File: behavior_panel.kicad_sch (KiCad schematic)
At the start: 32 parts, among them J1 Conn_01x16, Q1 Q_NPN_BEC, Q3 N-channel MOSFET, U1 LM2902, U2 LM317_3PinPackage, U3 SFH617A-1X007T

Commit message: Add documentation to schematic
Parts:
- removed Q1: Q_NPN_BEC, Package_TO_SOT_SMD:SOT-23, symbol Device:Q_NPN_BEC
- removed R19: 10k, Resistor_SMD:R_0402_1005Metric, symbol Device:R
- removed U3: SFH617A-1X007T, Package_DIP:SMDIP-4_W9.53mm_Clearance8mm, symbol Isolator:SFH617A-1X007T
- added C7: 0.1uF, Capacitor_SMD:C_0805_2012Metric, symbol Device:C
- added C8: 1uF, Capacitor_SMD:C_0603_1608Metric, symbol Device:C
- added D1: LED, symbol Device:LED
- added Q2: N-channel MOSFET, Package_TO_SOT_SMD:TO-252-2, symbol Transistor_FET:BUZ11
- added Q4: N MOSFET, Package_TO_SOT_SMD:TO-252-2, symbol Transistor_FET:BUZ11
- added Q5: Q_NPN_BCE, symbol Device:Q_NPN_BCE
- added R11, R13: 10k, Resistor_SMD:R_0402_1005Metric, symbol Device:R
- added R12, R14: 50, Resistor_SMD:R_0402_1005Metric, symbol Device:R
- added R15: 1k, symbol Device:R
- added R16: 100, symbol Device:R
- added SW1: SW_SPST, symbol Switch:SW_SPST
- added U3: LM317_3PinPackage, Package_TO_SOT_SMD:SOT-223, symbol Regulator_Linear:LM317_3PinPackage
- R10: value 220 -> 860
- R9: value 10k -> 100; footprint Resistor_SMD:R_0402_1005Metric -> Resistor_SMD:R_0805_2012Metric; MPN MF-RES-0402-10k -> MF-RES-0805-100
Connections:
- net +28V: now also C7.1, U3.3 (VI); no longer R9.2
- net 5V: now also R16.1
- net GND: now also R10.2, C7.2, C8.2, Q2.3 (S), Q4.3 (S), Q5.3 (E), R11.2, R13.2, SW1.1 (A)
- net PD_CTL: no longer R10.1
- net PD_OUT: no longer R9.1
- new net: Q5.1 (B), R15.2
- new net: R10.1, R9.2, U3.1 (ADJ)
- new net: D1.1 (K), Q5.2 (C)
- new net: D1.2 (A), R16.2
- new net 12V: C8.1, R12.1, R14.1, R9.1, U3.2 (VO)
- new net S1_CTL: Q2.1 (G), R11.1
- new net S1_IN: Q2.2 (D)
- new net S1_OUT: R12.2
- new net S2_CTL: Q4.1 (G), R13.1
- new net S2_IN: Q4.2 (D), R15.1, SW1.2 (B)
- new net S2_OUT: R14.2
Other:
- note added: "E1+ and E2+ go to the positive (anode) of the IR emitter. Cathode goes to ground. S1+ and S2+ go to either leg of the IR sensor. Other leg goes to ground. The RC circuit (R7 and C1) feeding to the positive leg of the op-amp form a lowpass circuit (1/2piRC) with a current cutoff of 160 Hz. The feedback capacitor (C3) stabilizes the response of the op-amp. O1 and O2 would feed into a BNC output tha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"
- note added: "Ground (negative) side of light should be connected to LT_IN. This circuit is designed for a 3W DC 12-24V LED lamp (e.g., SKU: P-AL-3W-E27-CW-1224 from 12vmonster.com). Positive end of light should be connected to 12-24V output. Feed LT_IN and 12V into a BNC connector so we can plug the light directly into the box."
- note added: "In general, I favor putting in PBC traces to a 2.54mm pin header that way we don't have to deal with identifying connectors that can be soldered onto a PCB. Instead, we put the connectors on the box itself, solder wires that terminate in a 2.54mm pin shroud, mount the PCB in the box, and then hook up the connectors to the PCB by plugging into the pin header."
- note added: "This is meant to be the control circuit for one of the solenoids. The solenoids need 12V for power (not sure what current draw is). S2_CTL can be connected to the NI digital output so that we can control via software. S2_OUT goes to the positive input to the solenoid. S2_IN comes from the negative input of the solenoid. When S2_CTL is high, this should allow current to flow through the MOSFET (an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"
- note added: "Voltage regulator circuit. It might be worth keeping both the 5 and 12V rails that way we can power the circuit from any DC power supply that is at least 14V (min dropout is ~1.2V)."
- note removed: "* R7+C1 form a lowpass circuit with fc = 1/(2piRC). Selected values give us a cutoff of 160 Hz. * C3 helps stabilize the response of the op-amp. * C5 and C17 are power supply bypass. Resistors * R1 selected to provide a current of less than 50mA to IR LED."
- moved on the sheet: C11, C12, H1, H2, H3, H4, R17, R18, U2

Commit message: Updated to include four power relays and four IR circuts
Went back to the through-hole, hand-solderable version.
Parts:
- removed C1, C2, C3, C4: 0.1uF, Capacitor_SMD:C_0603_1608Metric, symbol Device:C
- removed D1: LED, symbol Device:LED
- removed Q2, Q3: N-channel MOSFET, Package_TO_SOT_SMD:TO-252-2, symbol Transistor_FET:BUZ11
- removed Q4: N MOSFET, Package_TO_SOT_SMD:TO-252-2, symbol Transistor_FET:BUZ11
- removed Q5: Q_NPN_BCE, symbol Device:Q_NPN_BCE
- removed R1, R2: 100 0.25W, Resistor_SMD:R_1206_3216Metric, symbol Device:R
- removed R11, R13, R25, R3, R4, R5, R6, R7, R8: 10k, Resistor_SMD:R_0402_1005Metric, symbol Device:R
- removed R12, R14: 50, Resistor_SMD:R_0402_1005Metric, symbol Device:R
- removed R15: 1k, symbol Device:R
- removed R16: 100, symbol Device:R
- removed SW1: SW_SPST, symbol Switch:SW_SPST
- removed unit 1 of U1
- removed unit 2 of U1
- added J2, J3, J4: Conn_01x16, Connector_PinHeader_2.54mm:PinHeader_1x16_P2.54mm_Vertical, symbol Connector_Generic:Conn_01x16
- C1: renamed from C11; footprint Capacitor_SMD:C_0805_2012Metric -> Capacitor_THT:C_Rect_L7.0mm_W3.5mm_P5.00mm
- C2: renamed from C7; footprint Capacitor_SMD:C_0805_2012Metric -> Capacitor_THT:C_Rect_L7.0mm_W3.5mm_P5.00mm
- C3: renamed from C12; footprint Capacitor_SMD:C_0603_1608Metric -> Capacitor_THT:C_Rect_L7.0mm_W3.5mm_P5.00mm
- C4: renamed from C8; footprint Capacitor_SMD:C_0603_1608Metric -> Capacitor_THT:C_Rect_L7.0mm_W3.5mm_P5.00mm
- C5: footprint Capacitor_SMD:C_1206_3216Metric -> Capacitor_THT:C_Rect_L7.0mm_W3.5mm_P5.00mm
- C6: footprint Capacitor_SMD:C_0603_1608Metric -> Capacitor_THT:C_Rect_L7.0mm_W3.5mm_P5.00mm
- R1: renamed from R17; footprint Resistor_SMD:R_0805_2012Metric -> Resistor_THT:R_Axial_DIN0207_L6.3mm_D2.5mm_P7.62mm_Horizontal
- R2: renamed from R18; footprint Resistor_SMD:R_0805_2012Metric -> Resistor_THT:R_Axial_DIN0207_L6.3mm_D2.5mm_P7.62mm_Horizontal
- R3: renamed from R9; footprint Resistor_SMD:R_0805_2012Metric -> Resistor_THT:R_Axial_DIN0207_L6.3mm_D2.5mm_P7.62mm_Horizontal
- R4: renamed from R10; footprint Resistor_SMD:R_0805_2012Metric -> Resistor_THT:R_Axial_DIN0207_L6.3mm_D2.5mm_P7.62mm_Horizontal
- U1: renamed from U2; footprint Package_TO_SOT_SMD:SOT-223 -> Package_TO_SOT_THT:TO-220-3_Vertical
- U2: renamed from U3; footprint Package_TO_SOT_SMD:SOT-223 -> Package_TO_SOT_THT:TO-220-3_Vertical
- U3: renamed from U1; footprint Package_SO:TSSOP-14_4.4x5mm_P0.65mm -> Package_DIP:DIP-14_W7.62mm_LongPads
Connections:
- net E1+ is gone; now on net 5V: J1.15 (Pin_15)
- net E2+ is gone; now on net 5V: J1.16 (Pin_16)
- net LT_CTL is gone; now on net 5V: J1.4 (Pin_4)
- net LT_IN is gone; now on net 5V: J1.5 (Pin_5)
- net O1 is gone; now on net 5V: J1.11 (Pin_11)
- net O2 is gone; now on net 5V: J1.14 (Pin_14)
- net PD_CTL is gone; now on net 5V: J1.1 (Pin_1)
- net PD_OUT is gone; now on net 5V: J1.2 (Pin_2)
- net S1+ is gone; now on net 5V: J1.12 (Pin_12)
- net S2+ is gone; now on net 5V: J1.13 (Pin_13)
- net 12V: now also J2.1 (Pin_1), J2.10 (Pin_10), J2.11 (Pin_11), J2.12 (Pin_12), J2.13 (Pin_13), J2.14 (Pin_14), J2.15 (Pin_15), J2.16 (Pin_16), J2.2 (Pin_2), J2.3 (Pin_3), J2.4 (Pin_4), J2.5 (Pin_5), J2.6 (Pin_6), J2.7 (Pin_7), J2.8 (Pin_8), J2.9 (Pin_9)
- net 5V: now also J1.10 (Pin_10), J1.3 (Pin_3), J1.6 (Pin_6), J1.7 (Pin_7), J1.8 (Pin_8), J1.9 (Pin_9)
- net GND: now also J4.1 (Pin_1), J4.10 (Pin_10), J4.11 (Pin_11), J4.12 (Pin_12), J4.13 (Pin_13), J4.14 (Pin_14), J4.15 (Pin_15), J4.16 (Pin_16), J4.2 (Pin_2), J4.3 (Pin_3), J4.4 (Pin_4), J4.5 (Pin_5), J4.6 (Pin_6), J4.7 (Pin_7), J4.8 (Pin_8), J4.9 (Pin_9); no longer J1.10 (Pin_10), J1.6 (Pin_6), J1.8 (Pin_8), J1.9 (Pin_9)
- net +28V renamed VIN
- net VIN: now also J3.1 (Pin_1), J3.10 (Pin_10), J3.11 (Pin_11), J3.12 (Pin_12), J3.13 (Pin_13), J3.14 (Pin_14), J3.15 (Pin_15), J3.16 (Pin_16), J3.2 (Pin_2), J3.3 (Pin_3), J3.4 (Pin_4), J3.5 (Pin_5), J3.6 (Pin_6), J3.7 (Pin_7), J3.8 (Pin_8), J3.9 (Pin_9); no longer J1.3 (Pin_3), J1.7 (Pin_7)
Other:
- added sheet IR circuit (IR circuit.kicad_sch)
- added sheet IR circuit1 (IR circuit.kicad_sch)
- added sheet IR circuit2 (IR circuit.kicad_sch)
- added sheet IR circuit3 (IR circuit.kicad_sch)
- added sheet power control (power control.kicad_sch)
- added sheet power control2 (power control.kicad_sch)
- added sheet power control3 (power control.kicad_sch)
- added sheet power control4 (power control.kicad_sch)
- note removed: "Ground (negative) side of light should be connected to LT_IN. This circuit is designed for a 3W DC 12-24V LED lamp (e.g., SKU: P-AL-3W-E27-CW-1224 from 12vmonster.com). Positive end of light should be connected to 12-24V output. Feed LT_IN and 12V into a BNC connector so we can plug the light directly into the box."
- moved on the sheet: C1, C2, C3, C4, C5, C6, H1, H2, H3, H4, R1, R2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

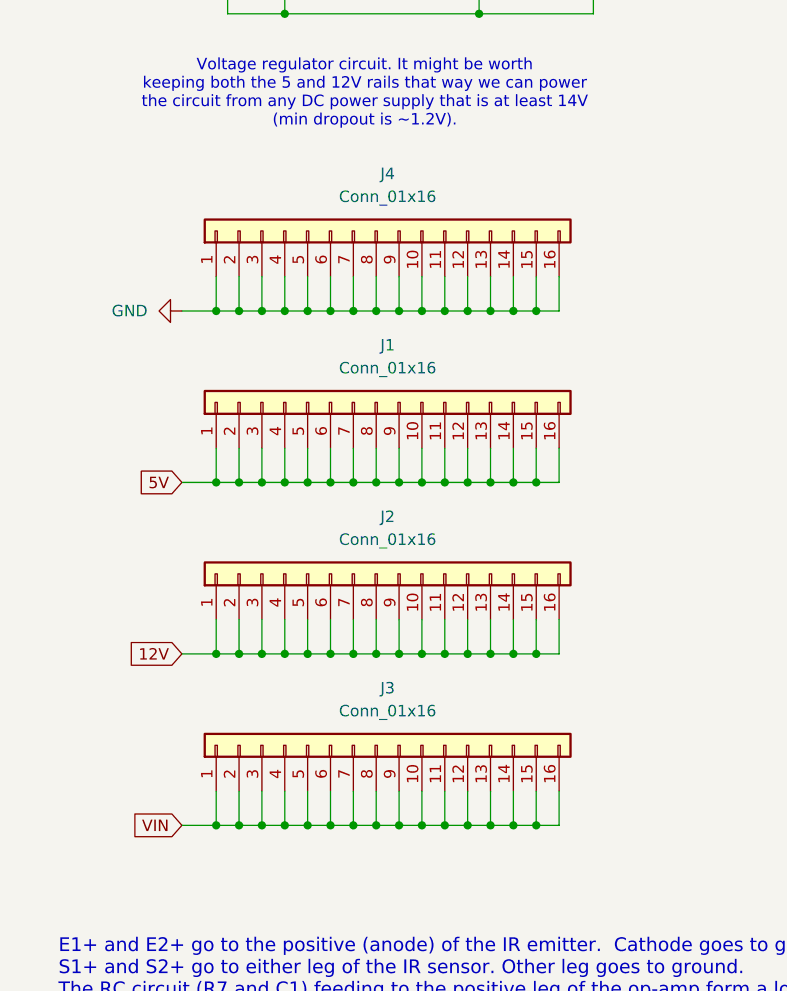
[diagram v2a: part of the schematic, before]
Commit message: Update connectors to be smaller
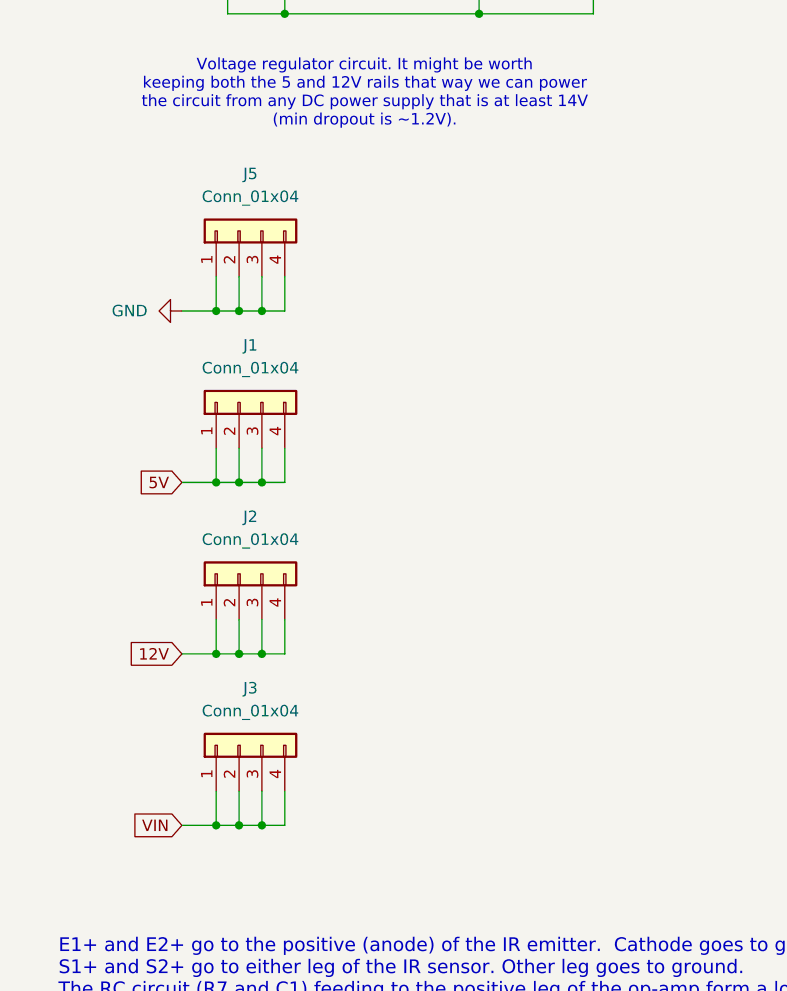
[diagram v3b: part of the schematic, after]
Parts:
- removed J1, J2, J3, J4: Conn_01x16, Connector_PinHeader_2.54mm:PinHeader_1x16_P2.54mm_Vertical, symbol Connector_Generic:Conn_01x16
- added J1, J2, J3, J5: Conn_01x04, Connector_PinHeader_2.54mm:PinHeader_1x04_P2.54mm_Vertical, symbol Connector_Generic:Conn_01x04
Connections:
- net 12V: now also J2.1 (Pin_1), J2.2 (Pin_2), J2.3 (Pin_3), J2.4 (Pin_4)
- net 5V: now also J1.1 (Pin_1), J1.2 (Pin_2), J1.3 (Pin_3), J1.4 (Pin_4)
- net GND: now also J5.1 (Pin_1), J5.2 (Pin_2), J5.3 (Pin_3), J5.4 (Pin_4)
- net VIN: now also J3.1 (Pin_1), J3.2 (Pin_2), J3.3 (Pin_3), J3.4 (Pin_4)

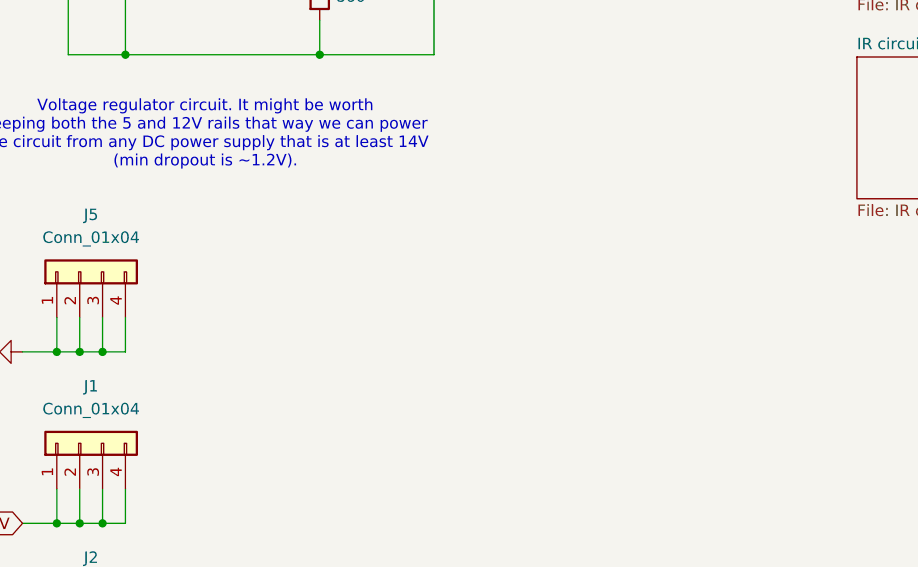
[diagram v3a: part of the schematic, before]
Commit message: Add more ground pins. Fix labels.
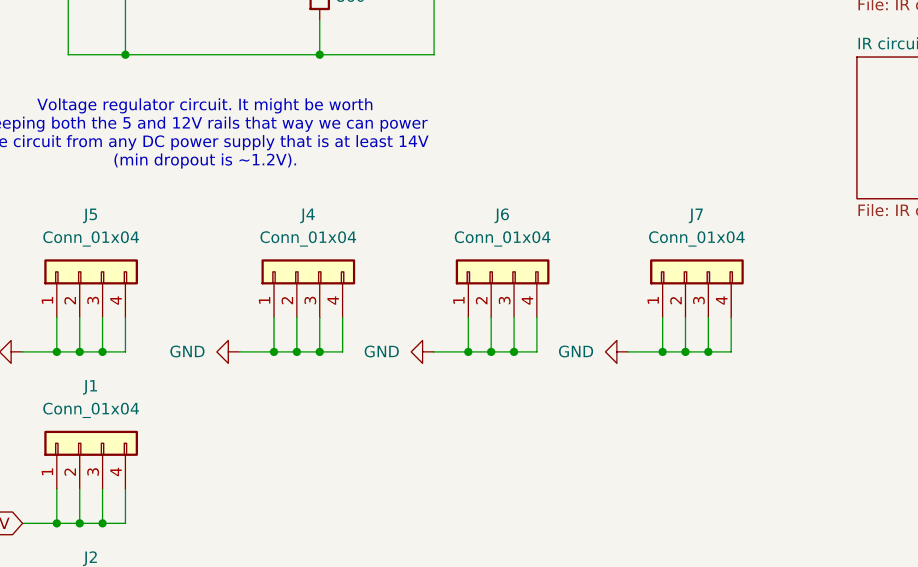
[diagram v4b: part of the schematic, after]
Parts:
- added J4, J6, J7: Conn_01x04, Connector_PinHeader_2.54mm:PinHeader_1x04_P2.54mm_Vertical, symbol Connector_Generic:Conn_01x04
- C1, C2: footprint Capacitor_THT:C_Rect_L7.0mm_W3.5mm_P5.00mm -> Capacitor_THT:C_Rect_L4.0mm_W2.5mm_P2.50mm; MPN MF-CAP-0805-0.1uF -> C315C104M5U5TA
- C6: footprint Capacitor_THT:C_Rect_L7.0mm_W3.5mm_P5.00mm -> Capacitor_THT:C_Rect_L4.0mm_W2.5mm_P2.50mm
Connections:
- net GND: now also J4.1 (Pin_1), J4.2 (Pin_2), J4.3 (Pin_3), J4.4 (Pin_4), J6.1 (Pin_1), J6.2 (Pin_2), J6.3 (Pin_3), J6.4 (Pin_4), J7.1 (Pin_1), J7.2 (Pin_2), J7.3 (Pin_3), J7.4 (Pin_4)
